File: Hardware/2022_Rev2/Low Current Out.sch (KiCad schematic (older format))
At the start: 54 parts

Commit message: Tiva implementation
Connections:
- net Anderson_BlackBox renamed Anderson_BBB
- net Anderson_Multimedia renamed Anderson_Multi
- net Current_Sense_BlackBox renamed Current_Sense_BBB
- net Current_Sense_Multimedia renamed Current_Sense_Multi
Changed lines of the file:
@@
 EESchema Schematic File Version 4
-LIBS:2022_Rev2-cache
 EELAYER 30 0
 EELAYER END
@@
 	4450 4500 4450 4450
 Text HLabel 4850 4800 3    50   Output ~ 0
-Current_Sense_BlackBox
+Current_Sense_BBB
 Text HLabel 4700 5450 3    50   Output ~ 0
-Anderson_BlackBox
+Anderson_BBB
 Wire Wire Line
 	4000 5450 4700 5450
@@
 	4300 2700 4300 2650
 Text HLabel 4700 3000 3    50   Output ~ 0
-Current_Sense_Multimedia
+Current_Sense_Multi
 Text HLabel 4550 3650 3    50   Output ~ 0
-Anderson_Multimedia
+Anderson_Multi
 Wire Wire Line
 	3850 3650 4550 3650

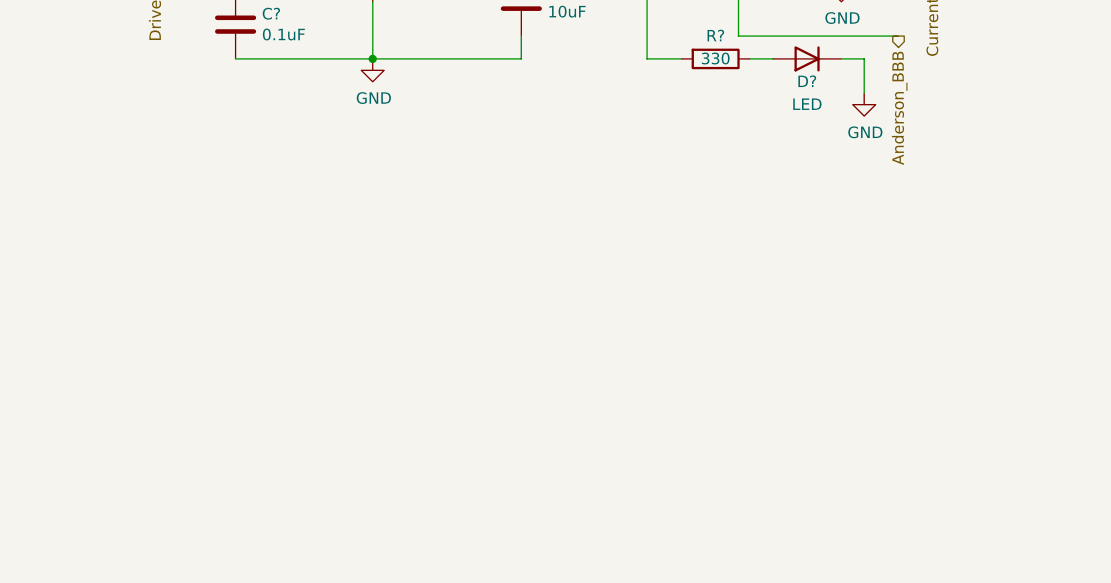
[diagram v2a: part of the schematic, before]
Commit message: change switch circuit naming + added more switch circuits.
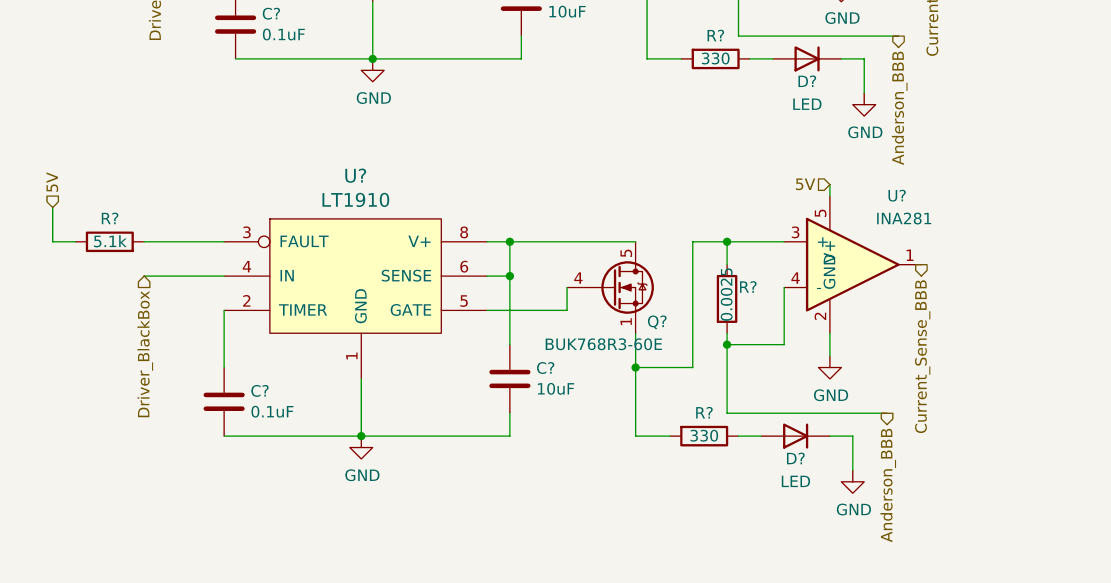
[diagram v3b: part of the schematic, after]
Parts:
- added C?: 0.1uF, symbol Device:C
- added C?: 10uF, symbol Device:C
- added D?: LED, symbol Device:D
- added Q?: BUK768R3-60E, Package_TO_SOT_SMD:LFPAK33, symbol Transistor_FET:BUK7M9R9-60EX
- added R?: 5.1k, symbol Device:R
- added R?: 330, symbol Device:R
- added R?: 0.0025, symbol Device:R
- added U?: LT1910, symbol 2022_Rev2-rescue:LT1910-MRDT_ICs
- added U?: INA281, Package_TO_SOT_SMD:SOT-23-5, symbol 2022_Rev2-rescue:INA281-MRDT_ICs
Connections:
- net 5V: now also R?.1, U?.5 (V+)
- net Anderson_BBB: now also R?.2, U?.4 (-)
- net Current_Sense_BBB: now also U?.1
- net Driver_BlackBox: now also U?.4 (IN)
- net GND: now also C?.2, C?.2, D?.1 (K), U?.1 (GND), U?.2 (GND)
- new net: R?.2, U?.3 (FAULT)
- new net: C?.1, U?.2 (TIMER)
- new net: Q?.4 (G), U?.5 (GATE)
- new net: C?.1, Q?.5 (D), U?.6 (SENSE), U?.8 (V+)
- new net: Q?.1 (S), Q?.2 (S), Q?.3 (S), R?.1, R?.2, U?.3 (+)
- new net: D?.2 (A), R?.1
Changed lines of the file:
@@
 Text HLabel 8750 4750 0    50   Input ~ 0
 5V
+$Comp
+L Device:R R?
+U 1 1 622D1853
+P 1250 6350
+F 0 "R?" V 1350 6350 50  0000 C CNN
+F 1 "5.1k" V 1250 6350 50  0000 C CNN
+F 2 "" V 1180 6350 50  0001 C CNN
+F 3 "~" H 1250 6350 50  0001 C CNN
+	1    1250 6350
+	0    -1   -1   0
+$EndComp
+$Comp
+L 2022_Rev2-rescue:LT1910-MRDT_ICs U?
+U 1 1 622D1859
+P 1950 6750
+F 0 "U?" H 2325 7437 60  0000 C CNN
+F 1 "LT1910" H 2325 7331 60  0000 C CNN
+F 2 "" H 1950 6750 60  0001 C CNN
+F 3 "" H 1950 6750 60  0001 C CNN
+	1    1950 6750
+	1    0    0    -1
+$EndComp
+$Comp
+L Device:C C?
+U 1 1 622D185F
+P 1750 7050
+F 0 "C?" H 1865 7096 50  0000 L CNN
+F 1 "0.1uF" H 1865 7005 50  0000 L CNN
+F 2 "" H 1788 6900 50  0001 C CNN
+F 3 "~" H 1750 7050 50  0001 C CNN
+	1    1750 7050
+	1    0    0    -1
+$EndComp
+$Comp
+L power:GND #PWR?
+U 1 1 622D1865
+P 2350 7200
+F 0 "#PWR?" H 2350 6950 50  0001 C CNN
+F 1 "GND" H 2355 7027 50  0000 C CNN
+F 2 "" H 2350 7200 50  0001 C CNN
+F 3 "" H 2350 7200 50  0001 C CNN
+	1    2350 7200
+	1    0    0    -1
+$EndComp
+$Comp
+L Device:C C?
+U 1 1 622D186B
+P 3000 6950
+F 0 "C?" H 3115 6996 50  0000 L CNN
+F 1 "10uF" H 3115 6905 50  0000 L CNN
+F 2 "" H 3038 6800 50  0001 C CNN
+F 3 "~" H 3000 6950 50  0001 C CNN
+	1    3000 6950
+	1    0    0    -1
+$EndComp
+$Comp
+L Transistor_FET:BUK7M9R9-60EX Q?
+U 1 1 622D1871
+P 3450 6550
+F 0 "Q?" H 3600 6400 50  0000 L CNN
+F 1 "BUK768R3-60E" H 3150 6300 50  0000 L CNN
+F 2 "Package_TO_SOT_SMD:LFPAK33" H 3650 6475 50  0001 L CIN
+F 3 "https://assets.nexperia.com/documents/data-sheet/BUK7M9R9-60E.pdf" V 3450 6550 50  0001 L CNN
+	1    3450 6550
+	1    0    0    -1
+$EndComp
+$Comp
+L Device:R R?
+U 1 1 622D1877
+P 3850 7200
+F 0 "R?" V 3750 7200 50  0000 C CNN
+F 1 "330" V 3850 7200 50  0000 C CNN
+F 2 "" V 3780 7200 50  0001 C CNN
+F 3 "~" H 3850 7200 50  0001 C CNN
+	1    3850 7200
+	0    1    1    0
+$EndComp
+$Comp
+L Device:D D?
+U 1 1 622D187D
+P 4250 7200
+F 0 "D?" H 4250 7300 50  0000 C CNN
+F 1 "LED" H 4250 7400 50  0000 C CNN
+F 2 "" H 4250 7200 50  0001 C CNN
+F 3 "~" H 4250 7200 50  0001 C CNN
+	1    4250 7200
+	-1   0    0    1
+$EndComp
+$Comp
+L 2022_Rev2-rescue:INA281-MRDT_ICs U?
+U 1 1 622D1883
+P 4400 6450
+F 0 "U?" H 4650 6750 50  0000 L CNN
+F 1 "INA281" H 4600 6650 50  0000 L CNN
+F 2 "Package_TO_SOT_SMD:SOT-23-5" H 4650 6650 50  0001 C CNN
+F 3 "https://www.ti.com/lit/ds/symlink/ina281.pdf?ts=1602621825218&ref_url=https%253A%252F%252Fwww.ti.com%252Fproduct%252FINA281" H 4650 6650 50  0001 C CNN
+	1    4400 6450
+	1    0    0    -1
+$EndComp
+Wire Wire Line
+	1400 6350 1750 6350
+Wire Wire Line
+	1750 6500 1400 6500
+Wire Wire Line
+	1750 6650 1750 6900
+Wire Wire Line
+	1750 7200 2350 7200
+Wire Wire Line
+	2350 6950 2350 7200
+Connection ~ 2350 7200
+Wire Wire Line
+	2350 7200 3000 7200
+Wire Wire Line
+	3000 7200 3000 7100
+Wire Wire Line
+	3000 6800 3000 6500
+Wire Wire Line
+	3000 6500 2900 6500
+Wire Wire Line
+	2900 6350 3000 6350
+Wire Wire Line
+	3000 6350 3000 6500
+Connection ~ 3000 6500
+Wire Wire Line
+	3250 6550 3250 6650
+Wire Wire Line
+	3250 6650 2900 6650
+Wire Wire Line
+	3000 6350 3550 6350
+Connection ~ 3000 6350
+Wire Wire Line
+	3550 6750 3550 6900
+Wire Wire Line
+	3550 7200 3700 7200
+Wire Wire Line
+	4000 7200 4100 7200
+Wire Wire Line
+	4400 7200 4500 7200
+Wire Wire Line
+	4500 7200 4500 7350
+$Comp
+L power:GND #PWR?
+U 1 1 622D189F
+P 4500 7350
+F 0 "#PWR?" H 4500 7100 50  0001 C CNN
+F 1 "GND" H 4505 7177 50  0000 C CNN
+F 2 "" H 4500 7350 50  0001 C CNN
+F 3 "" H 4500 7350 50  0001 C CNN
+	1    4500 7350
+	1    0    0    -1
+$EndComp
+$Comp
+L Device:R R?
+U 1 1 622D18A5
+P 3950 6600
+F 0 "R?" H 4000 6650 50  0000 L CNN
+F 1 "0.0025" V 3950 6500 50  0000 L CNN
+F 2 "" V 3880 6600 50  0001 C CNN
+F 3 "~" H 3950 6600 50  0001 C CNN
+	1    3950 6600
+	1    0    0    -1
+$EndComp
+Wire Wire Line
+	3550 6900 3800 6900
+Wire Wire Line
+	3800 6900 3800 6350
+Wire Wire Line
+	3800 6350 3950 6350
+Connection ~ 3550 6900
+Wire Wire Line
+	3550 6900 3550 7200
+Wire Wire Line
+	3950 6350 3950 6450
+Connection ~ 3950 6350
+Wire Wire Line
+	3950 6350 4200 6350
+Wire Wire Line
+	3950 6750 3950 6800
+Wire Wire Line
+	3950 6800 4200 6800
+Wire Wire Line
+	4200 6800 4200 6550
+Connection ~ 3950 6800
+$Comp
+L power:GND #PWR?
+U 1 1 622D18B7
+P 4400 6850
+F 0 "#PWR?" H 4400 6600 50  0001 C CNN
+F 1 "GND" H 4405 6677 50  0000 C CNN
+F 2 "" H 4400 6850 50  0001 C CNN
+F 3 "" H 4400 6850 50  0001 C CNN
+	1    4400 6850
+	1    0    0    -1
+$EndComp
+Wire Wire Line
+	3950 6800 3950 7100
+Wire Wire Line
+	4400 6750 4400 6850
+Wire Wire Line
+	4400 6150 4400 6100
+Text HLabel 4800 6450 3    50   Output ~ 0
+Current_Sense_BBB
+Text HLabel 4650 7100 3    50   Output ~ 0
+Anderson_BBB
+Wire Wire Line
+	3950 7100 4650 7100
+Wire Wire Line
+	1100 6350 1000 6350
+Wire Wire Line
+	1000 6350 1000 6200
+Text HLabel 1400 6500 3    50   Input ~ 0
+Driver_BlackBox
+Text HLabel 1000 6200 1    50   Input ~ 0
+5V
+Text HLabel 4400 6100 0    50   Input ~ 0
+5V
 $EndSCHEMATC

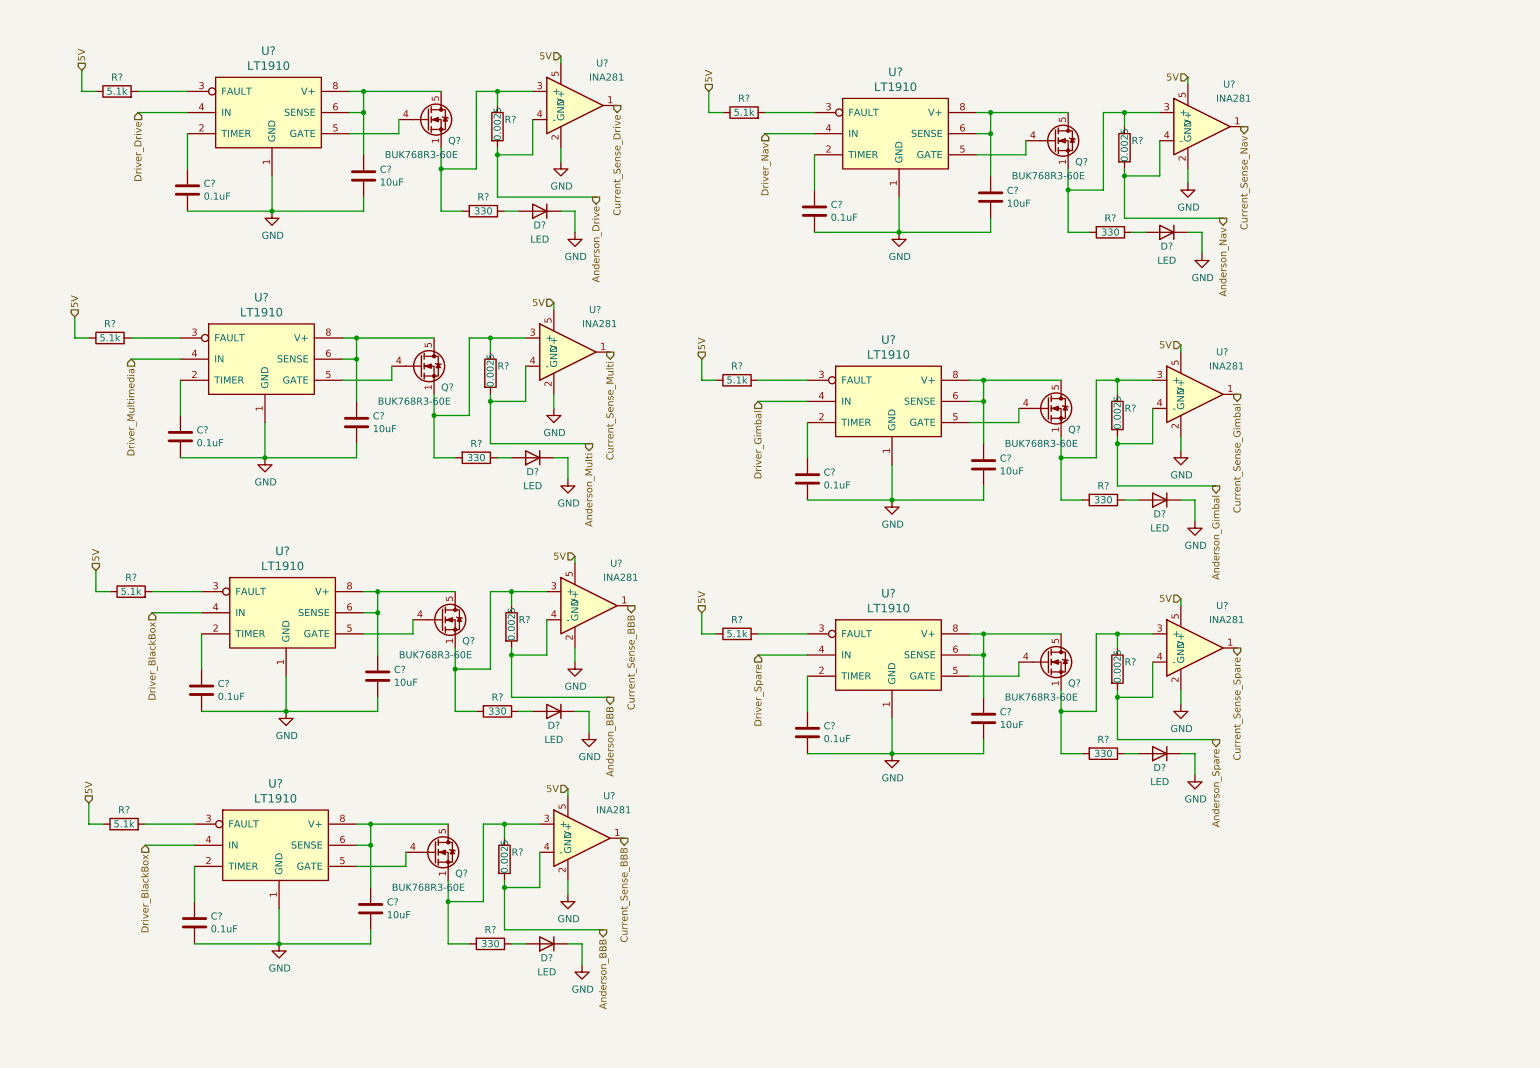
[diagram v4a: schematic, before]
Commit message: 12v switch circuits added
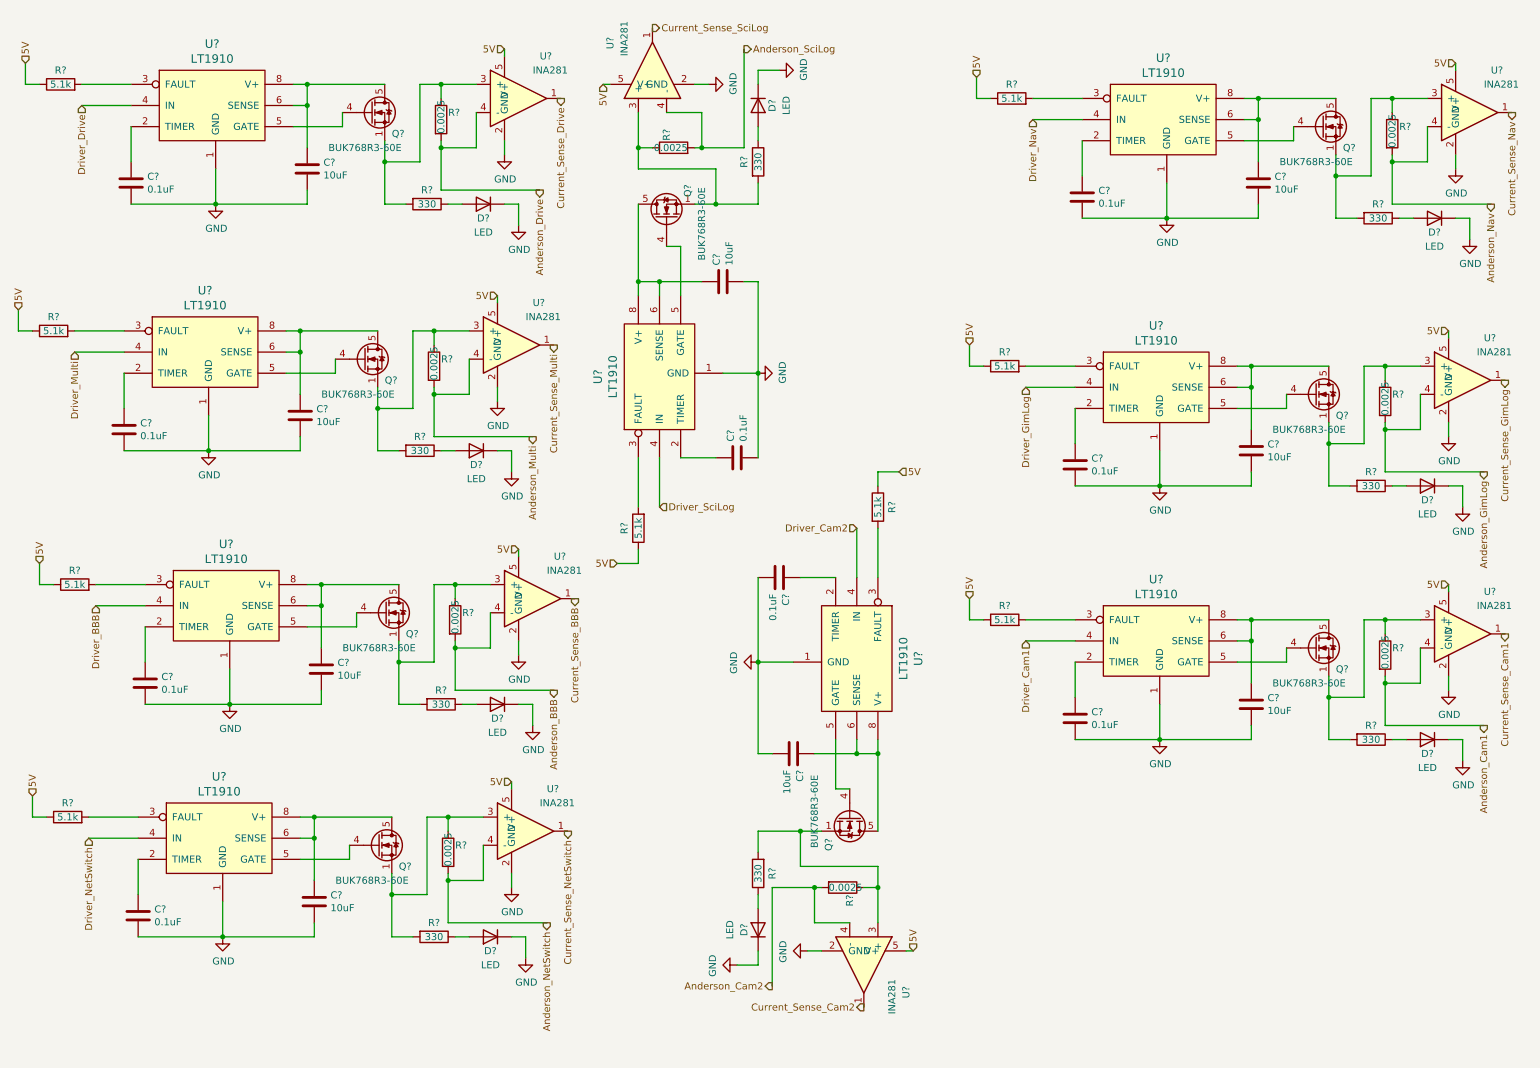
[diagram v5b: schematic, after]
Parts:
- added C? (x2): 0.1uF, symbol Device:C
- added C? (x2): 10uF, symbol Device:C
- added D? (x2): LED, symbol Device:D
- added Q? (x2): BUK768R3-60E, Package_TO_SOT_SMD:LFPAK33, symbol Transistor_FET:BUK7M9R9-60EX
- added R? (x2): 5.1k, symbol Device:R
- added R? (x2): 330, symbol Device:R
- added R? (x2): 0.0025, symbol Device:R
- added U? (x2): LT1910, symbol 2022_Rev2-rescue:LT1910-MRDT_ICs
- added U? (x2): INA281, Package_TO_SOT_SMD:SOT-23-5, symbol 2022_Rev2-rescue:INA281-MRDT_ICs
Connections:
- net 5V: now also R?.1, R?.1, U?.5 (V+), U?.5 (V+)
- net Anderson_BBB: no longer R?.2, U?.4 (-)
- net Current_Sense_BBB: no longer U?.1
- net GND: now also C?.2, C?.2, C?.2, C?.2, D?.1 (K), D?.1 (K), U?.1 (GND), U?.1 (GND), U?.2 (GND), U?.2 (GND)
- net Anderson_Gimbal renamed Anderson_GimLog
- net Anderson_Spare renamed Anderson_Cam1
- net Current_Sense_Gimbal renamed Current_Sense_GimLog
- net Current_Sense_Spare renamed Current_Sense_Cam1
- net Driver_BlackBox renamed Driver_BBB
- net Driver_BBB: no longer U?.4 (IN)
- net Driver_Gimbal renamed Driver_GimLog
- net Driver_Multimedia renamed Driver_Multi
- net Driver_Spare renamed Driver_Cam1
- new net: R?.2, U?.3 (FAULT) (x2)
- new net: C?.1, U?.2 (TIMER) (x2)
- new net: Q?.4 (G), U?.5 (GATE) (x2)
- new net: C?.1, Q?.5 (D), U?.6 (SENSE), U?.8 (V+) (x2)
- new net: Q?.1 (S), Q?.2 (S), Q?.3 (S), R?.1, R?.2, U?.3 (+) (x2)
- new net: D?.2 (A), R?.1 (x2)
- new net Anderson_Cam2: R?.2, U?.4 (-)
- new net Anderson_NetSwitch: R?.2, U?.4 (-)
- new net Anderson_SciLog: R?.2, U?.4 (-)
- new net Current_Sense_Cam2: U?.1
- new net Current_Sense_NetSwitch: U?.1
- new net Current_Sense_SciLog: U?.1
- new net Driver_Cam2: U?.4 (IN)
- new net Driver_NetSwitch: U?.4 (IN)
- new net Driver_SciLog: U?.4 (IN)
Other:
- moved on the sheet: C?, D?, Q?, R?, U?
